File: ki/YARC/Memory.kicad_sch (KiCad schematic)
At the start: 18 parts, among them U14 74LS20, U18 AS6C6264, U20 74HC00, U21 74LS08, U22 74LS139, U23 74LS32, U24 AS6C6264, U25 74HC245, U26 74LS157, U27 AS6C6264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

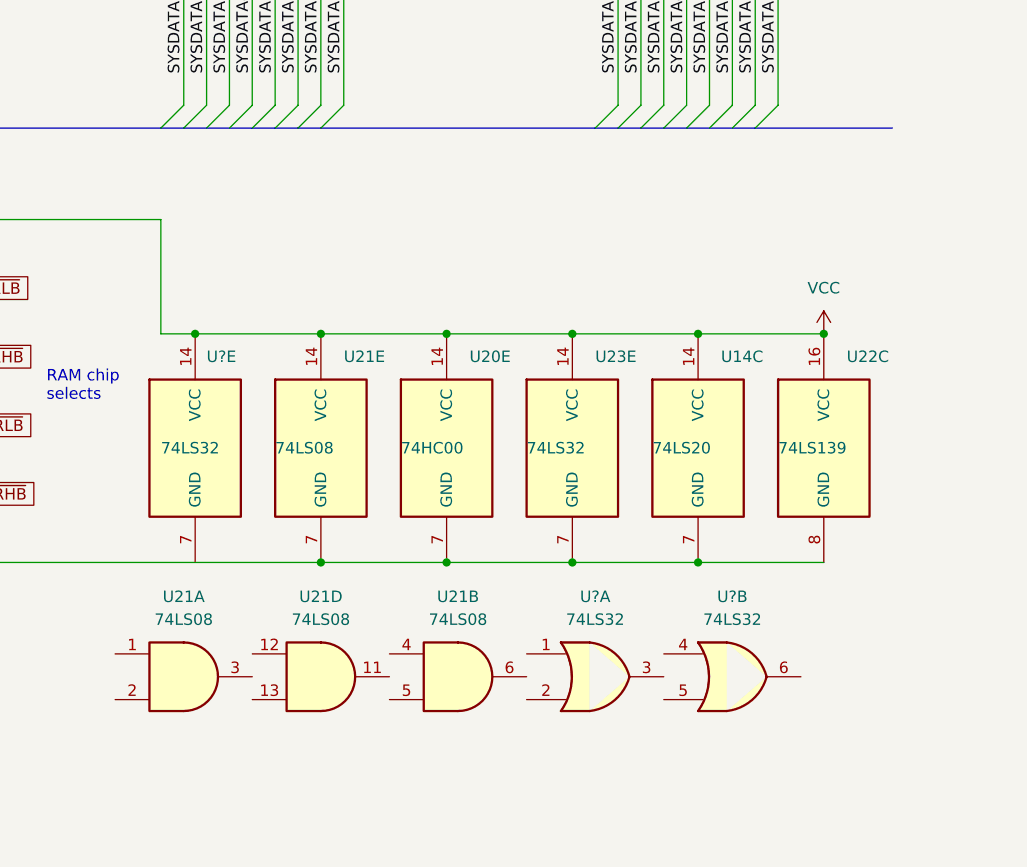
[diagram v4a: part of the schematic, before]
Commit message: Nano IR clock and mem enable changes documented in Ki, Ftz, and port_task.h
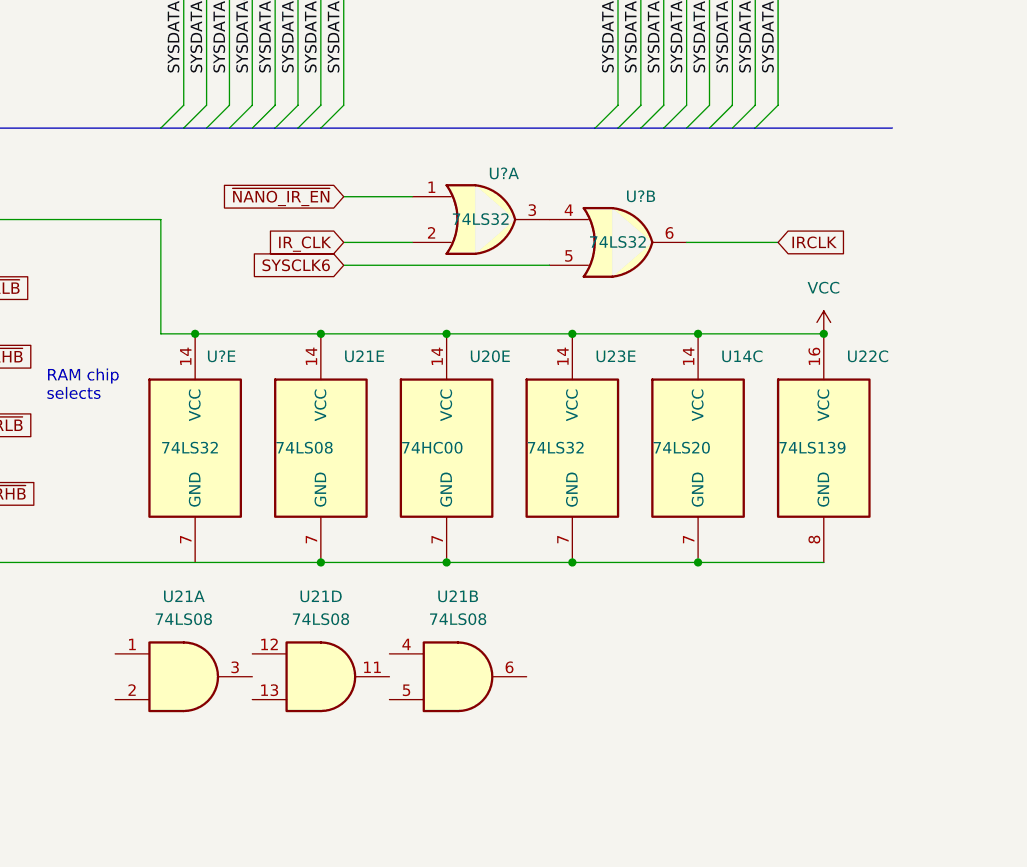
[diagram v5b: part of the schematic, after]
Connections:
- net SYSCLK6: now also U?.5
- net at U?.4: now also U?.3
- net IRCLK: now reaches U?.6
- net ~{NANO_IR_EN}: now reaches U?.1
- net IR_CLK: now reaches U?.2
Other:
- moved on the sheet: U?A, U?B
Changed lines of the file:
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@@
+    (stroke (width 0) (type default) (color 0 0 0 0))
+  )
+  (wire (pts (xy 226.06 137.16) (xy 203.2 137.16))
     (stroke (width 0) (type default) (color 0 0 0 0))
   )
@@
     (stroke (width 0) (type default) (color 0 0 0 0))
   )
+  (wire (pts (xy 241.3 134.62) (xy 251.46 134.62))
+    (stroke (width 0) (type default) (color 0 0 0 0))
+  )
   (wire (pts (xy 50.8 180.34) (xy 66.04 180.34))
     (stroke (width 0) (type default) (color 0 0 0 0))
@@
     (stroke (width 0) (type default) (color 0 0 0 0))
   )
+  (wire (pts (xy 203.2 134.62) (xy 210.82 134.62))
+    (stroke (width 0) (type default) (color 0 0 0 0))
+  )
   (wire (pts (xy 83.82 129.54) (xy 83.82 134.62))
     (stroke (width 0) (type default) (color 0 0 0 0))
@@
   )
   (bus (pts (xy 231.14 15.24) (xy 264.16 15.24))
+    (stroke (width 0) (type default) (color 0 0 0 0))
+  )
+  (wire (pts (xy 203.2 129.54) (xy 210.82 129.54))
     (stroke (width 0) (type default) (color 0 0 0 0))
   )
@@
     )
   )
+  (global_label "IR_CLK" (shape input) (at 203.2 134.62 180) (fields_autoplaced)
+    (effects (font (size 1.27 1.27)) (justify right))
+    (property "Intersheet References" "${INTERSHEET_REFS}" (id 0) (at 194.3764 134.5406 0)
+      (effects (font (size 1.27 1.27)) (justify right) hide)
+    )
+  )
   (global_label "RAM{slash}~{IO}" (shape input) (at 73.66 78.74 0) (fields_autoplaced)
     (effects (font (size 1.27 1.27)) (justify left))
@@
     )
   )
+  (global_label "SYSCLK6" (shape input) (at 203.2 137.16 180) (fields_autoplaced)
+    (effects (font (size 1.27 1.27)) (justify right))
+    (property "Intersheet References" "${INTERSHEET_REFS}" (id 0) (at 192.5017 137.0806 0)
+      (effects (font (size 1.27 1.27)) (justify right) hide)
+    )
+  )
   (global_label "~{SEL_LRHB}" (shape input) (at 157.48 147.32 0) (fields_autoplaced)
     (effects (font (size 1.27 1.27)) (justify left))
@@
     )
   )
+  (global_label "IRCLK" (shape input) (at 251.46 134.62 0) (fields_autoplaced)
+    (effects (font (size 1.27 1.27)) (justify left))
+    (property "Intersheet References" "${INTERSHEET_REFS}" (id 0) (at 259.316 134.5406 0)
+      (effects (font (size 1.27 1.27)) (justify left) hide)
+    )
+  )
   (global_label "~{SEL_HRHB}" (shape input) (at 157.48 162.56 0) (fields_autoplaced)
     (effects (font (size 1.27 1.27)) (justify left))
@@
     (property "Intersheet References" "${INTERSHEET_REFS}" (id 0) (at 98.0864 91.3606 0)
       (effects (font (size 1.27 1.27)) (justify left) hide)
+    )
+  )
+  (global_label "~{NANO_IR_EN}" (shape input) (at 203.2 129.54 180) (fields_autoplaced)
+    (effects (font (size 1.27 1.27)) (justify right))
+    (property "Intersheet References" "${INTERSHEET_REFS}" (id 0) (at 189.4174 129.4606 0)
+      (effects (font (size 1.27 1.27)) (justify right) hide)
     )
   )
@@
     (pin "7")
   )
-  (symbol (lib_id "74xx:74LS32") (at 246.38 182.88 0) (unit 2)
-    (in_bom yes) (on_board yes) (fields_autoplaced)
-    (property "Reference" "U?" (id 0) (at 246.38 173.99 0))
-    (property "Value" "74LS32" (id 1) (at 246.38 176.53 0))
-    (property "Footprint" "" (id 2) (at 246.38 182.88 0)
-      (effects (font (size 1.27 1.27)) hide)
-    )
-    (property "Datasheet" "http://www.ti.com/lit/gpn/sn74LS32" (id 3) (at 246.38 182.88 0)
+  (symbol (lib_id "74xx:74LS32") (at 233.68 134.62 0) (unit 2)
+    (in_bom yes) (on_board yes)
+    (property "Reference" "U?" (id 0) (at 236.22 129.54 0))
+    (property "Value" "74LS32" (id 1) (at 233.68 134.62 0))
+    (property "Footprint" "" (id 2) (at 233.68 134.62 0)
+      (effects (font (size 1.27 1.27)) hide)
+    )
+    (property "Datasheet" "http://www.ti.com/lit/gpn/sn74LS32" (id 3) (at 233.68 134.62 0)
       (effects (font (size 1.27 1.27)) hide)
     )
@@
     (pin "7")
   )
-  (symbol (lib_id "74xx:74LS32") (at 231.14 182.88 0) (unit 1)
-    (in_bom yes) (on_board yes) (fields_autoplaced)
-    (property "Reference" "U?" (id 0) (at 231.14 173.99 0))
-    (property "Value" "74LS32" (id 1) (at 231.14 176.53 0))
-    (property "Footprint" "" (id 2) (at 231.14 182.88 0)
-      (effects (font (size 1.27 1.27)) hide)
-    )
-    (property "Datasheet" "http://www.ti.com/lit/gpn/sn74LS32" (id 3) (at 231.14 182.88 0)
-      (effects (font (size 1.27 1.27)) hide)
-    )
+  (symbol (lib_id "74xx:74LS32") (at 218.44 132.08 0) (unit 1)
+    (in_bom yes) (on_board yes)
+    (property "Reference" "U?" (id 0) (at 220.98 127 0))
+    (property "Value" "74LS32" (id 1) (at 218.44 132.08 0))
+    (property "Footprint" "" (id 2) (at 218.44 132.08 0)
+      (effects (font (size 1.27 1.27)) hide)
+    )
+    (property "Datasheet" "http://www.ti.com/lit/gpn/sn74LS32" (id 3) (at 218.44 132.08 0)
+      (effects (font (size 1.27 1.27)) hide)
+    )

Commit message: Continuing work on microcode control
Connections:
- net IRCLK is gone; now on net IR_CLK: U?.6
- net IR_CLK: no longer U?.2
- new net WCS_IR_CLK: U?.2
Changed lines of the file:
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@@
     )
   )
-  (global_label "IR_CLK" (shape input) (at 203.2 134.62 180) (fields_autoplaced)
+  (global_label "WCS_IR_CLK" (shape input) (at 203.2 134.62 180) (fields_autoplaced)
     (effects (font (size 1.27 1.27)) (justify right))
-    (property "Intersheet References" "${INTERSHEET_REFS}" (id 0) (at 194.3764 134.5406 0)
+    (property "Intersheet References" "${INTERSHEET_REFS}" (id 0) (at 189.4779 134.5406 0)
       (effects (font (size 1.27 1.27)) (justify right) hide)
     )
@@
     )
   )
-  (global_label "IRCLK" (shape input) (at 251.46 134.62 0) (fields_autoplaced)
+  (global_label "IR_CLK" (shape input) (at 251.46 134.62 0) (fields_autoplaced)
     (effects (font (size 1.27 1.27)) (justify left))
-    (property "Intersheet References" "${INTERSHEET_REFS}" (id 0) (at 259.316 134.5406 0)
+    (property "Intersheet References" "${INTERSHEET_REFS}" (id 0) (at 260.2836 134.5406 0)
       (effects (font (size 1.27 1.27)) (justify left) hide)
     )

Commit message: More wiring fixes and firmware development
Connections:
- net WCS_IR_CLK: now also U21.13; no longer U?.2
- net ~{NANO_IR_EN}: now also U21.12; no longer U?.1
- net at U21.11: now also U?.4
- net IR_RD_CLK: now reaches U?.3
- net IR_RD_CLK: no longer U?.4
- new net SYSCLK: U?.1
- new net ~{IR_RD}: U?.2
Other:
- moved on the sheet: U21A, U21B, U21D, U?A
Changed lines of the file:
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@@
+    (stroke (width 0) (type default) (color 0 0 0 0))
+  )
+  (wire (pts (xy 203.2 134.62) (xy 208.28 134.62))
     (stroke (width 0) (type default) (color 0 0 0 0))
   )
@@
     (stroke (width 0) (type default) (color 0 0 0 0))
   )
+  (wire (pts (xy 203.2 129.54) (xy 208.28 129.54))
+    (stroke (width 0) (type default) (color 0 0 0 0))
+  )
   (bus (pts (xy 114.3 66.04) (xy 116.84 66.04))
     (stroke (width 0) (type default) (color 0 0 0 0))
@@
     (stroke (width 0) (type default) (color 0 0 0 0))
   )
-  (wire (pts (xy 203.2 134.62) (xy 210.82 134.62))
-    (stroke (width 0) (type default) (color 0 0 0 0))
-  )
   (wire (pts (xy 83.82 129.54) (xy 83.82 134.62))
     (stroke (width 0) (type default) (color 0 0 0 0))
@@
     (stroke (width 0) (type default) (color 0 0 0 0))
   )
+  (wire (pts (xy 223.52 132.08) (xy 226.06 132.08))
+    (stroke (width 0) (type default) (color 0 0 0 0))
+  )
   (wire (pts (xy 241.3 68.58) (xy 241.3 81.28))
     (stroke (width 0) (type default) (color 0 0 0 0))
@@
   )
   (bus (pts (xy 231.14 15.24) (xy 264.16 15.24))
-    (stroke (width 0) (type default) (color 0 0 0 0))
-  )
-  (wire (pts (xy 203.2 129.54) (xy 210.82 129.54))
     (stroke (width 0) (type default) (color 0 0 0 0))
   )
@@
     )
   )
+  (global_label "~{IR_RD}" (shape input) (at 226.06 182.88 180) (fields_autoplaced)
+    (effects (font (size 1.27 1.27)) (justify right))
+    (property "Intersheet References" "${INTERSHEET_REFS}" (id 0) (at 218.2645 182.8006 0)
+      (effects (font (size 1.27 1.27)) (justify right) hide)
+    )
+  )
   (global_label "~{MEMWR_CLK}" (shape input) (at 152.4 50.8 270) (fields_autoplaced)
     (effects (font (size 1.27 1.27)) (justify right))
@@
     )
   )
+  (global_label "SYSCLK" (shape input) (at 226.06 177.8 180) (fields_autoplaced)
+    (effects (font (size 1.27 1.27)) (justify right))
+    (property "Intersheet References" "${INTERSHEET_REFS}" (id 0) (at 216.5712 177.7206 0)
+      (effects (font (size 1.27 1.27)) (justify right) hide)
+    )
+  )
   (global_label "~{CROSS_EN}" (shape input) (at 128.27 198.12 0) (fields_autoplaced)
     (effects (font (size 1.27 1.27)) (justify left))
@@
     (property "Intersheet References" "${INTERSHEET_REFS}" (id 0) (at 189.4174 129.4606 0)
       (effects (font (size 1.27 1.27)) (justify right) hide)
+    )
+  )
+  (global_label "IR_RD_CLK" (shape input) (at 241.3 180.34 0) (fields_autoplaced)
+    (effects (font (size 1.27 1.27)) (justify left))
+    (property "Intersheet References" "${INTERSHEET_REFS}" (id 0) (at 253.6312 180.2606 0)
+      (effects (font (size 1.27 1.27)) (justify left) hide)
     )
   )
@@
     (pin "1")
   )
-  (symbol (lib_id "74xx:74LS08") (at 185.42 182.88 0) (unit 1)
-    (in_bom yes) (on_board yes) (fields_autoplaced)
-    (property "Reference" "U21" (id 0) (at 185.42 173.99 0))
-    (property "Value" "74LS08" (id 1) (at 185.42 176.53 0))
-    (property "Footprint" "" (id 2) (at 185.42 182.88 0)
-      (effects (font (size 1.27 1.27)) hide)
-    )
-    (property "Datasheet" "http://www.ti.com/lit/gpn/sn74LS08" (id 3) (at 185.42 182.88 0)
+  (symbol (lib_id "74xx:74LS08") (at 170.18 182.88 0) (unit 1)
+    (in_bom yes) (on_board yes)
+    (property "Reference" "U21" (id 0) (at 175.26 177.8 0))
+    (property "Value" "74LS08" (id 1) (at 170.18 182.88 0))
+    (property "Footprint" "" (id 2) (at 170.18 182.88 0)
+      (effects (font (size 1.27 1.27)) hide)
+    )
+    (property "Datasheet" "http://www.ti.com/lit/gpn/sn74LS08" (id 3) (at 170.18 182.88 0)
       (effects (font (size 1.27 1.27)) hide)
     )
@@
     (pin "9")
   )
-  (symbol (lib_id "74xx:74LS08") (at 200.66 182.88 0) (unit 4)
-    (in_bom yes) (on_board yes) (fields_autoplaced)
-    (property "Reference" "U21" (id 0) (at 200.66 173.99 0))
-    (property "Value" "74LS08" (id 1) (at 200.66 176.53 0))
-    (property "Footprint" "" (id 2) (at 200.66 182.88 0)
-      (effects (font (size 1.27 1.27)) hide)
-    )
-    (property "Datasheet" "http://www.ti.com/lit/gpn/sn74LS08" (id 3) (at 200.66 182.88 0)
+  (symbol (lib_id "74xx:74LS08") (at 215.9 132.08 0) (unit 4)
+    (in_bom yes) (on_board yes)
+    (property "Reference" "U21" (id 0) (at 218.44 127 0))
+    (property "Value" "74LS08" (id 1) (at 215.9 132.08 0))
+    (property "Footprint" "" (id 2) (at 215.9 132.08 0)
+      (effects (font (size 1.27 1.27)) hide)
+    )
+    (property "Datasheet" "http://www.ti.com/lit/gpn/sn74LS08" (id 3) (at 215.9 132.08 0)
       (effects (font (size 1.27 1.27)) hide)
     )
@@
     (pin "7")
   )
-  (symbol (lib_id "74xx:74LS32") (at 218.44 132.08 0) (unit 1)
-    (in_bom yes) (on_board yes)
-    (property "Reference" "U?" (id 0) (at 220.98 127 0))
-    (property "Value" "74LS32" (id 1) (at 218.44 132.08 0))
-    (property "Footprint" "" (id 2) (at 218.44 132.08 0)
-      (effects (font (size 1.27 1.27)) hide)
-    )
-    (property "Datasheet" "http://www.ti.com/lit/gpn/sn74LS32" (id 3) (at 218.44 132.08 0)
+  (symbol (lib_id "74xx:74LS32") (at 233.68 180.34 0) (unit 1)
+    (in_bom yes) (on_board yes)
+    (property "Reference" "U?" (id 0) (at 236.22 175.26 0))
+    (property "Value" "74LS32" (id 1) (at 233.68 180.34 0))
+    (property "Footprint" "" (id 2) (at 233.68 180.34 0)
+      (effects (font (size 1.27 1.27)) hide)
+    )
+    (property "Datasheet" "http://www.ti.com/lit/gpn/sn74LS32" (id 3) (at 233.68 180.34 0)
       (effects (font (size 1.27 1.27)) hide)
     )
@@
     (pin "3")
   )
-  (symbol (lib_id "74xx:74LS08") (at 215.9 182.88 0) (unit 2)
-    (in_bom yes) (on_board yes) (fields_autoplaced)
-    (property "Reference" "U21" (id 0) (at 215.9 173.99 0))
-    (property "Value" "74LS08" (id 1) (at 215.9 176.53 0))
-    (property "Footprint" "" (id 2) (at 215.9 182.88 0)
-      (effects (font (size 1.27 1.27)) hide)
-    )
-    (property "Datasheet" "http://www.ti.com/lit/gpn/sn74LS08" (id 3) (at 215.9 182.88 0)
-      (effects (font (size 1.27 1.27)) hide)
-    )
+  (symbol (lib_id "74xx:74LS08") (at 190.5 182.88 0) (unit 2)
+    (in_bom yes) (on_board yes)
+    (property "Reference" "U21" (id 0) (at 195.58 177.8 0))
+    (property "Value" "74LS08" (id 1) (at 190.5 182.88 0))
+    (property "Footprint" "" (id 2) (at 190.5 182.88 0)
+      (effects (font (size 1.27 1.27)) hide)
+    )
+    (property "Datasheet" "http://www.ti.com/lit/gpn/sn74LS08" (id 3) (at 190.5 182.88 0)
+      (effects (font (size 1.27 1.27)) hide)
+    )

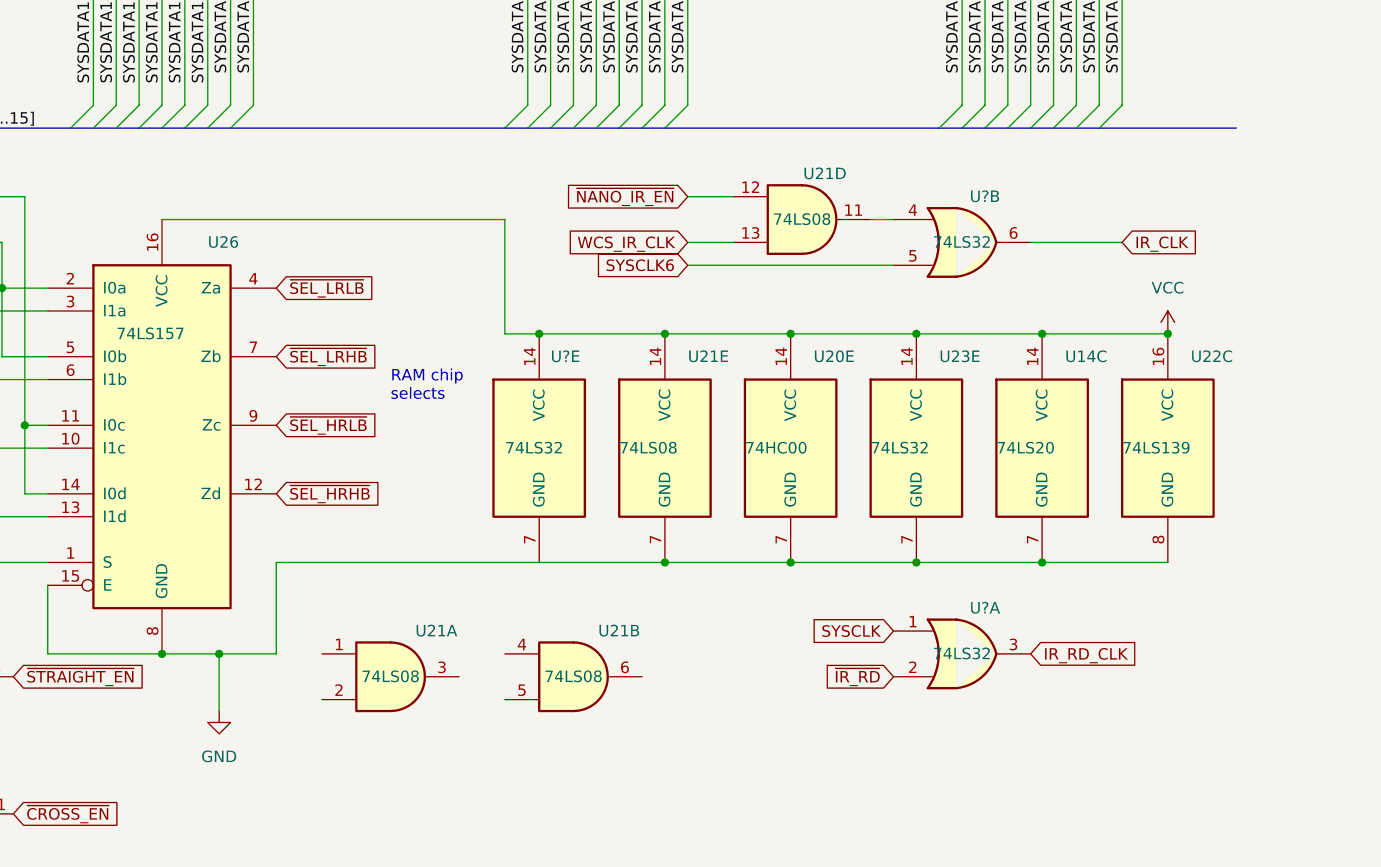
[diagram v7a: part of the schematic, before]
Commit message: All the changes related to the mid-December 2022 K register problem
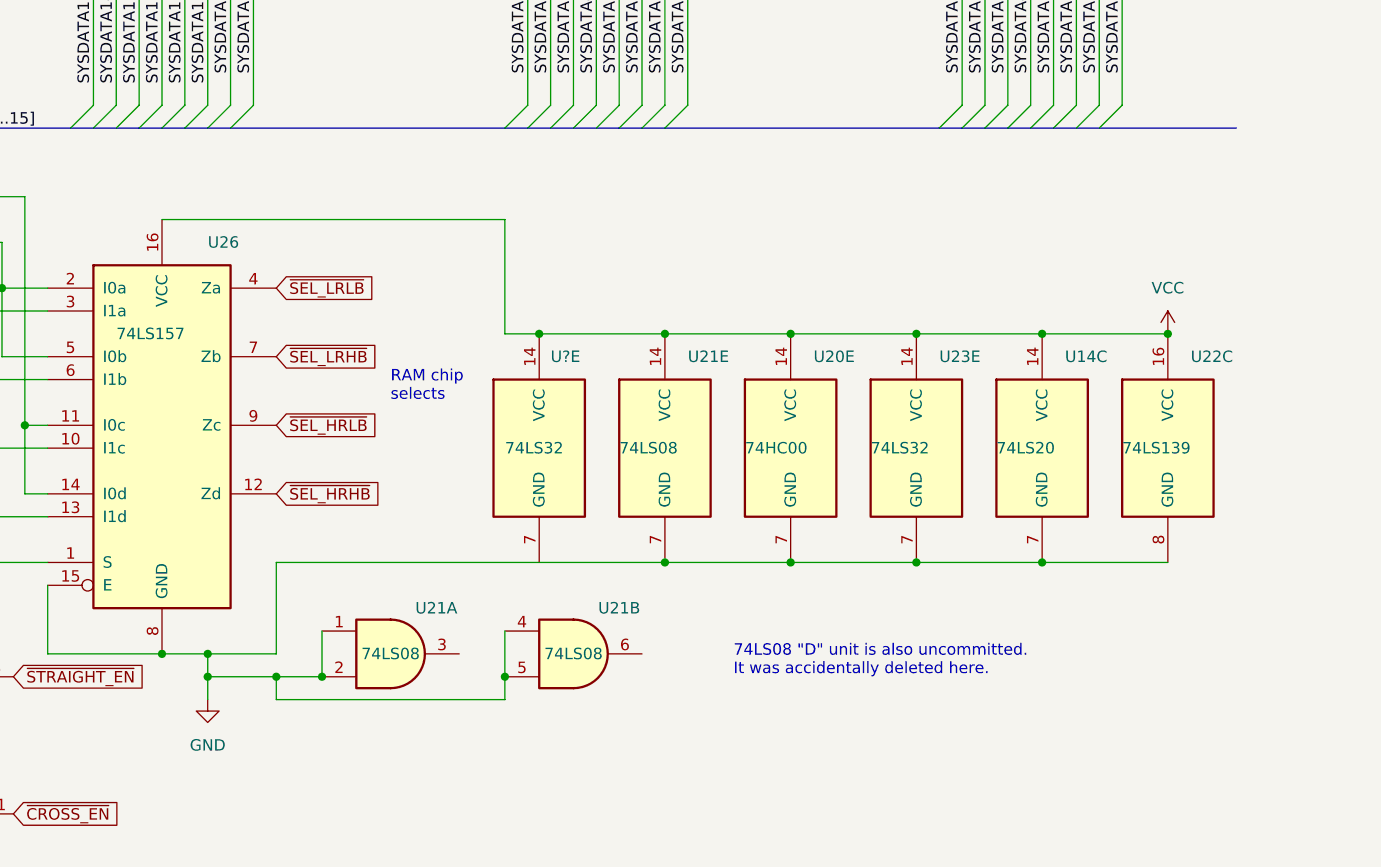
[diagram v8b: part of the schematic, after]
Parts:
- removed unit 4 of U21
- removed U? (x2): 74LS32, symbol 74xx:74LS32
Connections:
- net GND: now also U21.1, U21.2, U21.4, U21.5
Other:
- note added: "74LS08 "D" unit is also uncommitted. It was accidentally deleted here."
- moved on the sheet: U21A, U21B
